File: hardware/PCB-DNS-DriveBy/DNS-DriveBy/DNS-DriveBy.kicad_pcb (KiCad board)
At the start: 2 copper layers, 76 x 40 mm, 16 parts, among them J1 JST 2.0, Q1 2N3904, Q2 2N3904, SW1 SW_SPST, U1 NEO-6M, U2 D1 Mini

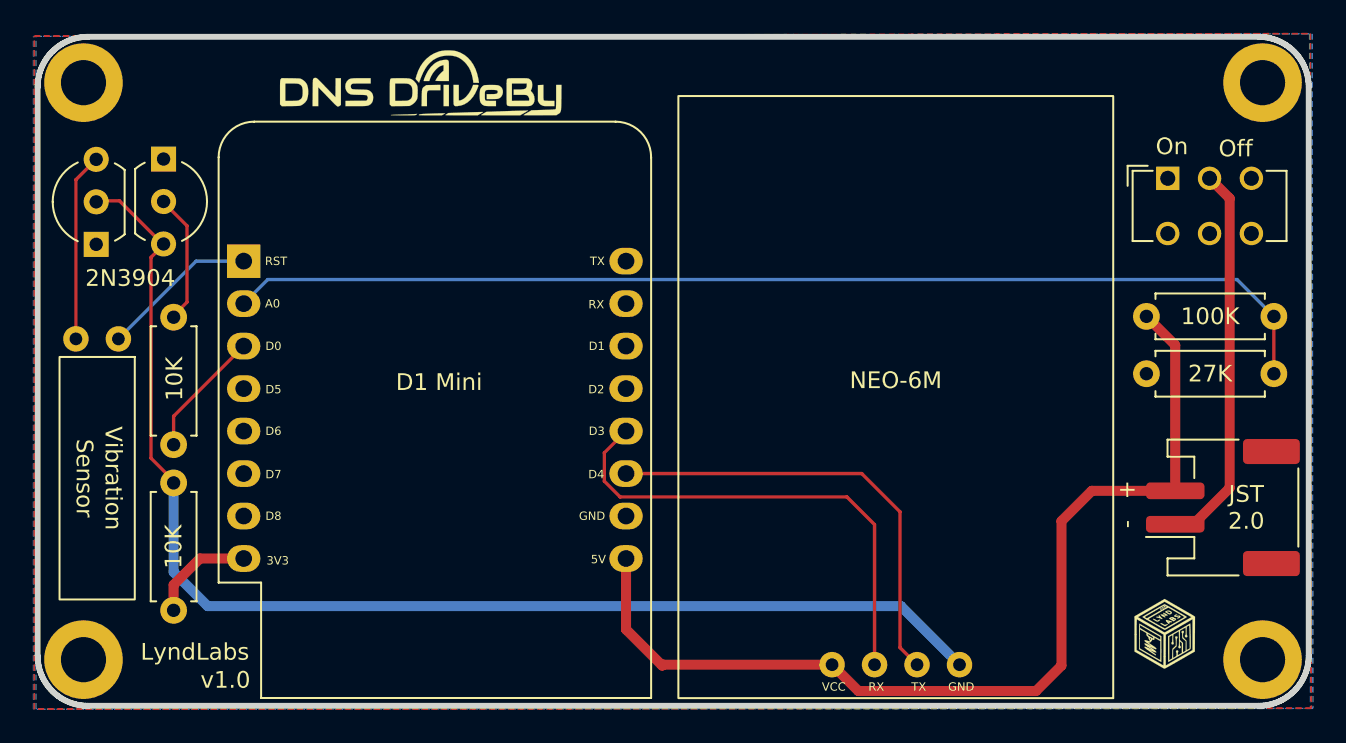
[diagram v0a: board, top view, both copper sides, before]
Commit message: PCB improvements: screen + serial breakout, re-routeable GPS pins
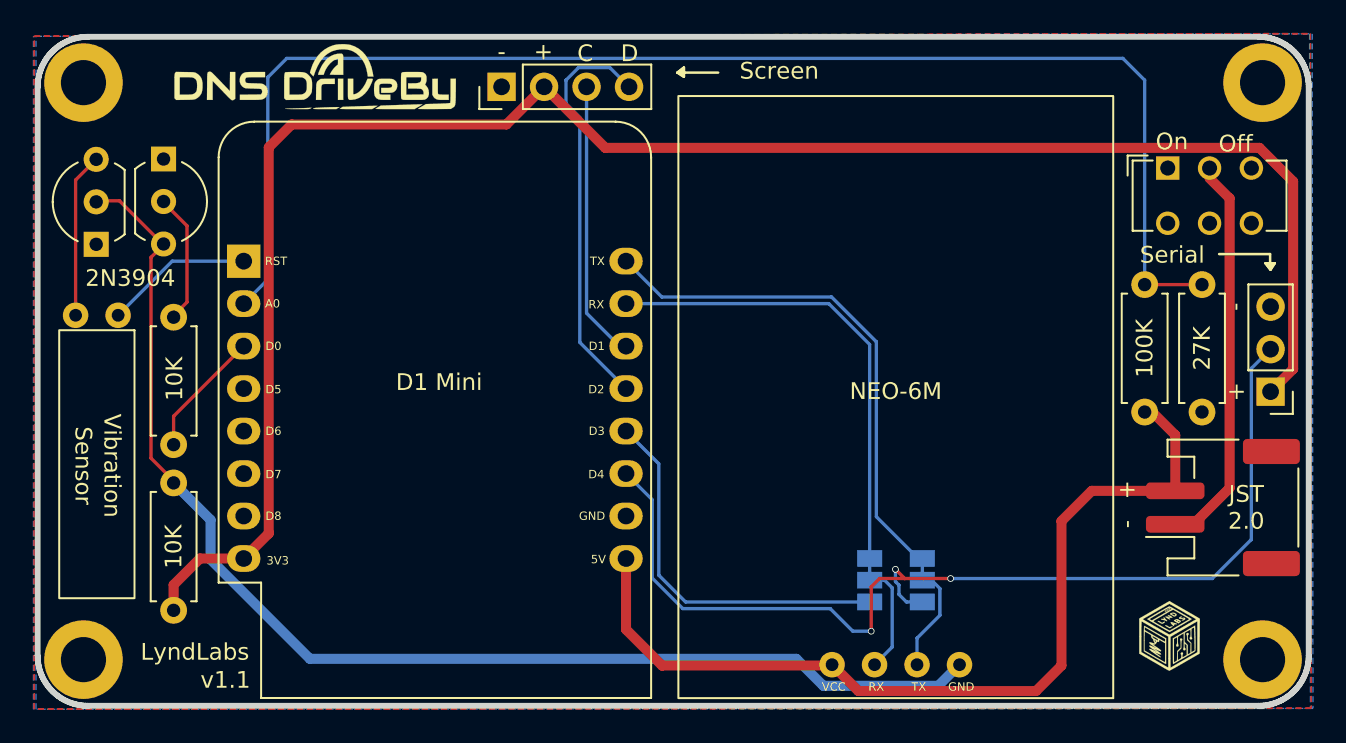
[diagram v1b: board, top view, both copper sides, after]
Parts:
- added J2: Conn_01x04, Connector_PinHeader_2.54mm:PinHeader_1x04_P2.54mm_Vertical, F.Cu at (28.5, 3.75)
- added J3: Conn_01x03, Connector_PinHeader_2.54mm:PinHeader_1x03_P2.54mm_Vertical, F.Cu at (74.5, 22.0)
- added RX: SolderJumper-3_P1.3mm_Open_Pad1.0x1.5mm, Jumper:SolderJumper-3_P1.3mm_Open_Pad1.0x1.5mm, B.Cu at (50.5, 33.2)
- added TX: SolderJumper-3_P1.3mm_Open_Pad1.0x1.5mm, Jumper:SolderJumper-3_P1.3mm_Open_Pad1.0x1.5mm, B.Cu at (53.7, 33.2)
- moved R4 6.85 mm to (70.4, 15.6), turned to -90 degrees
- moved Ref** 6.33 mm to (26.4, 20.1)
- moved R3 5.72 mm to (67.0, 23.2), turned to 90 degrees
- moved S1 1.41 mm to (4.30, 25.7)
- moved SW1 0.61 mm to (68.3, 8.61)
- renumbered U2 to U1, U1 to U2
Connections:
- U1 pad 11: GPS_TX -> TX1
- U1 pad 12: GPS_RX -> unconnected-(U1-Pad12)
- U1 pad 13: unconnected-(U2-Pad13) -> SDA
- U1 pad 14: unconnected-(U2-Pad14) -> SCL
- U1 pad 15: unconnected-(U2-Pad15) -> GPS_RX
- U1 pad 16: unconnected-(U2-Pad16) -> GPS_TX
- U1 pad 4: unconnected-(U2-Pad4) -> SCK
- U1 pad 5: unconnected-(U2-Pad5) -> MISO
- U1 pad 6: unconnected-(U2-Pad6) -> MOSI
- U1 pad 7: unconnected-(U2-Pad7) -> SS
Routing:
- net +3V3: track 6.37 -> 109.8 mm
- net TX1: track 0.00 -> 63.7 mm, vias 0 -> 3
- net SDA: track 0.00 -> 24.5 mm
- net unconnected-(U1-Pad12): track 0.00 -> 22.7 mm
- net SCL: track 0.00 -> 16.7 mm
- net A0: track 66.5 -> 83.2 mm
- net GPS_TX: track 26.9 -> 38.9 mm
- net GPS_RX: track 29.1 -> 35.9 mm
- net +BATT: track 59.8 -> 54.6 mm
- net Net-(Q2-Pad3): track 11.2 -> 9.83 mm
- net GPS-: track 74.7 -> 74.0 mm
- net RST: track 9.42 -> 8.85 mm
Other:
- board text added: "C"
- board text added: "D"
- board text added: "D3"
- board text added: "D4"
- board text added: "GPS Pins"
- board text added: "RX"
- board text added: "SSD1306 SH1106"
- board text added: "Screen"
- board text added: "Serial"
- board text added: "TX"
- board text added: "dnsdriveby.com"
- board text added: "v1.1"
- board text removed: "alexlynd.com/projects/DNS-DriveBy"
- board text removed: "v1.0"

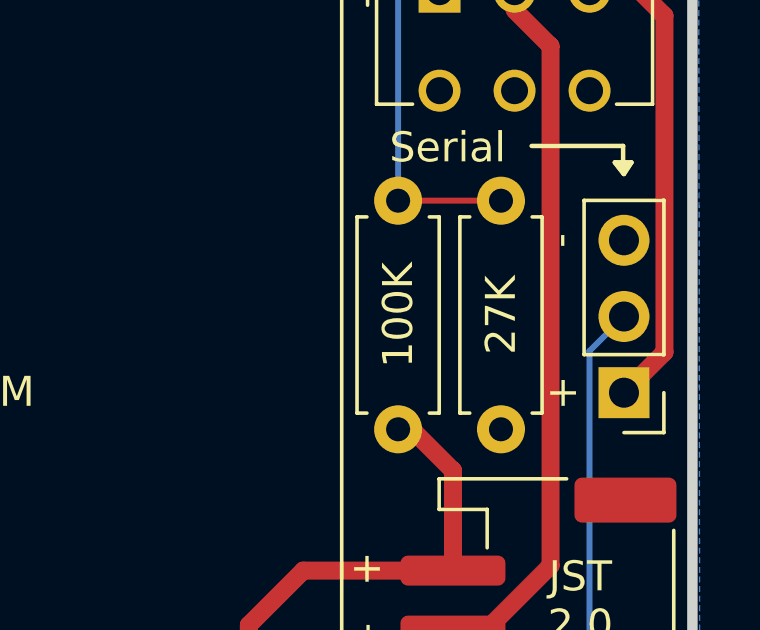
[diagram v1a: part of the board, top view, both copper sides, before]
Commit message: update resistor values
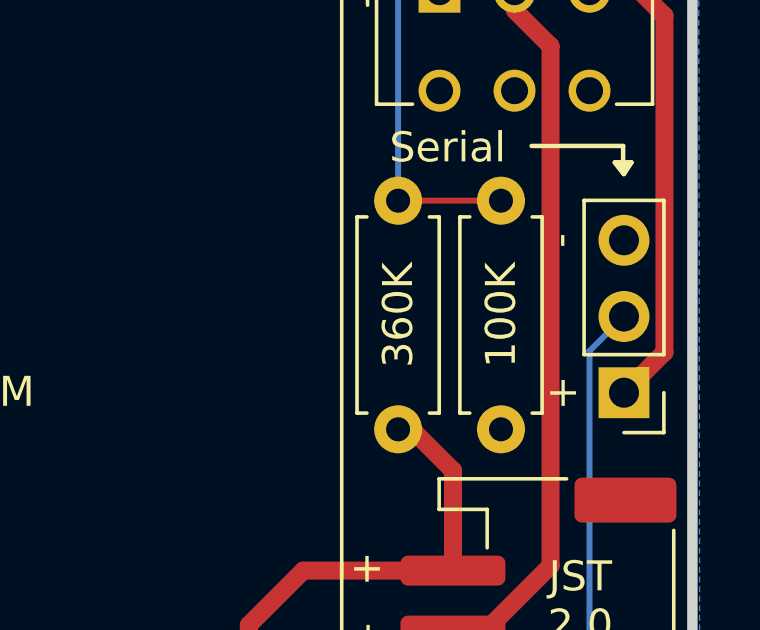
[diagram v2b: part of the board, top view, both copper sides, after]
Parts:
- R3: value 100K -> 360K
- R4: value 27K -> 100K
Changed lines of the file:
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@@
       (effects (font (size 1 1) (thickness 0.15)))
     )
-    (fp_text value "27K" (at 3.81 0 -270) (layer "F.SilkS")
+    (fp_text value "100K" (at 3.81 0 -270) (layer "F.SilkS")
       (effects (font (size 1 1) (thickness 0.15)))
     )
@@
       (effects (font (size 1 1) (thickness 0.15)))
     )
-    (fp_text value "100K" (at 3.81 0 90) (layer "F.SilkS")
-      (effects (font (size 1 1) (thickness 0.15)))
-    )
+    (fp_text value "360K" (at 3.81 0 90) (layer "F.SilkS")
+      (effects (font (size 1 1) (thickness 0.15)))
+    )

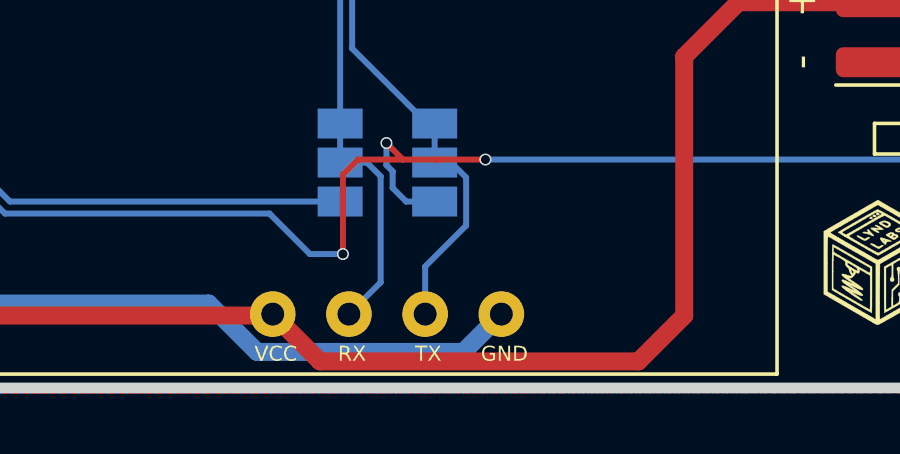
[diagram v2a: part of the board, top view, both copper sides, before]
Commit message: add GPS ground jumper bypass
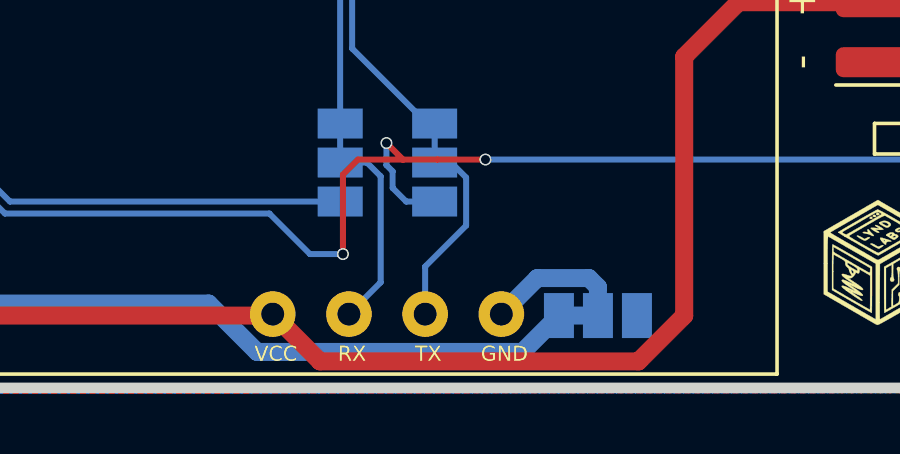
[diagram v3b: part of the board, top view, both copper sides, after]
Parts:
- added GPS GND: SolderJumper-3_P1.3mm_Open_Pad1.0x1.5mm, Jumper:SolderJumper-3_P1.3mm_Open_Pad1.0x1.5mm, B.Cu at (59.1, 38.4)
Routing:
- net GPS-: track 74.0 -> 82.0 mm
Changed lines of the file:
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@@
     )
     (pad_to_mask_clearance 0)
+    (grid_origin 54.3052 32.5882)
     (pcbplotparams
       (layerselection 0x00010fc_ffffffff)
@@
   )
   (footprint "Jumper:SolderJumper-3_P1.3mm_Open_Pad1.0x1.5mm" (layer "B.Cu")
+    (at 59.1 38.35 180)
+    (descr "SMD Solder 3-pad Jumper, 1x1.5mm Pads, 0.3mm gap, open")
+    (tags "solder jumper open")
+    (attr exclude_from_pos_files exclude_from_bom)
+    (fp_text reference "GPS GND" (at -6.051 -0.004) (layer "B.SilkS")
+      (effects (font (size 1 1) (thickness 0.15)) (justify mirror))
+    )
+    (fp_text value "SolderJumper-3_P1.3mm_Open_Pad1.0x1.5mm" (at 0 -2) (layer "B.Fab")
+      (effects (font (size 1 1) (thickness 0.15)) (justify mirror))
+    )
+    (fp_line (start 2.05 -1) (end -2.05 -1) (layer "B.SilkS") (width 0.12))
+    (fp_line (start -1.4 -2) (end -1.2 -2) (layer "B.SilkS") (width 0.12))
+    (fp_line (start -1.75 -1.5) (end -0.85 -1.5) (layer "B.SilkS") (width 0.12))
+    (fp_line (start -2.05 -1) (end -2.05 1) (layer "B.SilkS") (width 0.12))
+    (fp_line (start 2.05 1) (end 2.05 -1) (layer "B.SilkS") (width 0.12))
+    (fp_line (start -1.55 -1.75) (end -1.05 -1.75) (layer "B.SilkS") (width 0.12))
+    (fp_line (start -2.05 1) (end 2.05 1) (layer "B.SilkS") (width 0.12))
+    (fp_line (start -1.3 -1) (end -1.3 -1.5) (layer "B.SilkS") (width 0.12))
+    (fp_line (start 2.3 -1.25) (end 2.3 1.25) (layer "B.CrtYd") (width 0.05))
+    (fp_line (start -2.3 1.25) (end -2.3 -1.25) (layer "B.CrtYd") (width 0.05))
+    (fp_line (start -2.3 1.25) (end 2.3 1.25) (layer "B.CrtYd") (width 0.05))
+    (fp_line (start 2.3 -1.25) (end -2.3 -1.25) (layer "B.CrtYd") (width 0.05))
+    (pad "1" smd rect (at -1.3 0 180) (size 1 1.5) (layers "B.Cu" "B.Mask")
+      (net 2 "GND"))
+    (pad "2" smd rect (at 0 0 180) (size 1 1.5) (layers "B.Cu" "B.Mask")
+      (net 10 "GPS-"))
+    (pad "3" smd rect (at 1.3 0 180) (size 1 1.5) (layers "B.Cu" "B.Mask")
+      (net 10 "GPS-"))
+  )
+  (footprint "Jumper:SolderJumper-3_P1.3mm_Open_Pad1.0x1.5mm" (layer "B.Cu")
     (at 53.6575 33.25 -90)
     (descr "SMD Solder 3-pad Jumper, 1x1.5mm Pads, 0.3mm gap, open")
@@
       (net 20 "TX1"))
   )
+  (gr_line (start 58.4454 39.3634) (end 58.4454 37.3634) (layer "B.SilkS") (width 0.15))
   (gr_line (start 52.65 32.6) (end 54.65 32.6) (layer "B.SilkS") (width 0.15))
   (gr_line (start 49.5 32.6) (end 51.5 32.6) (layer "B.SilkS") (width 0.15))
@@
   (segment (start 7.5376 25.9526) (end 8.89 27.305) (width 0.2) (layer "F.Cu") (net 10))
   (segment (start 5.656 10.5664) (end 8.2876 13.198) (width 0.2) (layer "F.Cu") (net 10))
+  (segment (start 58.799511 37.100489) (end 59.1 37.400978) (width 0.6) (layer "B.Cu") (net 10))
+  (segment (start 46.124753 37.95) (end 17.040002 37.95) (width 0.6) (layer "B.Cu") (net 10))
   (segment (start 11.1 29.642) (end 8.89 27.432) (width 0.6) (layer "B.Cu") (net 10))
+  (segment (start 56.587289 39.562711) (end 47.737464 39.562711) (width 0.6) (layer "B.Cu") (net 10))
+  (segment (start 57.8 38.35) (end 59.1 38.35) (width 0.6) (layer "B.Cu") (net 10))
+  (segment (start 59.1 37.400978) (end 59.1 38.35) (width 0.6) (layer "B.Cu") (net 10))
+  (segment (start 11.1 32.009998) (end 11.1 29.642) (width 0.6) (layer "B.Cu") (net 10))
+  (segment (start 55.88 38.3012) (end 57.080711 37.100489) (width 0.6) (layer "B.Cu") (net 10))
+  (segment (start 57.080711 37.100489) (end 58.799511 37.100489) (width 0.6) (layer "B.Cu") (net 10))
   (segment (start 47.737464 39.562711) (end 46.124753 37.95) (width 0.6) (layer "B.Cu") (net 10))
+  (segment (start 57.8 38.35) (end 56.587289 39.562711) (width 0.6) (layer "B.Cu") (net 10))
   (segment (start 17.040002 37.95) (end 11.1 32.009998) (width 0.6) (layer "B.Cu") (net 10))
-  (segment (start 55.88 38.3012) (end 54.618489 39.562711) (width 0.6) (layer "B.Cu") (net 10))
-  (segment (start 54.618489 39.562711) (end 47.737464 39.562711) (width 0.6) (layer "B.Cu") (net 10))
-  (segment (start 46.124753 37.95) (end 17.040002 37.95) (width 0.6) (layer "B.Cu") (net 10))
-  (segment (start 11.1 32.009998) (end 11.1 29.642) (width 0.6) (layer "B.Cu") (net 10))
   (segment (start 3.03 9.3172) (end 4.26 8.0872) (width 0.2) (layer "F.Cu") (net 11))
   (segment (start 3.03 17.4104) (end 3.03 9.3172) (width 0.2) (layer "F.Cu") (net 11))
